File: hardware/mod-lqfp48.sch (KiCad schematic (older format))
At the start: 11 parts, among them J1 Target, U1 STM32F103C8Tx, Y1 8MHz

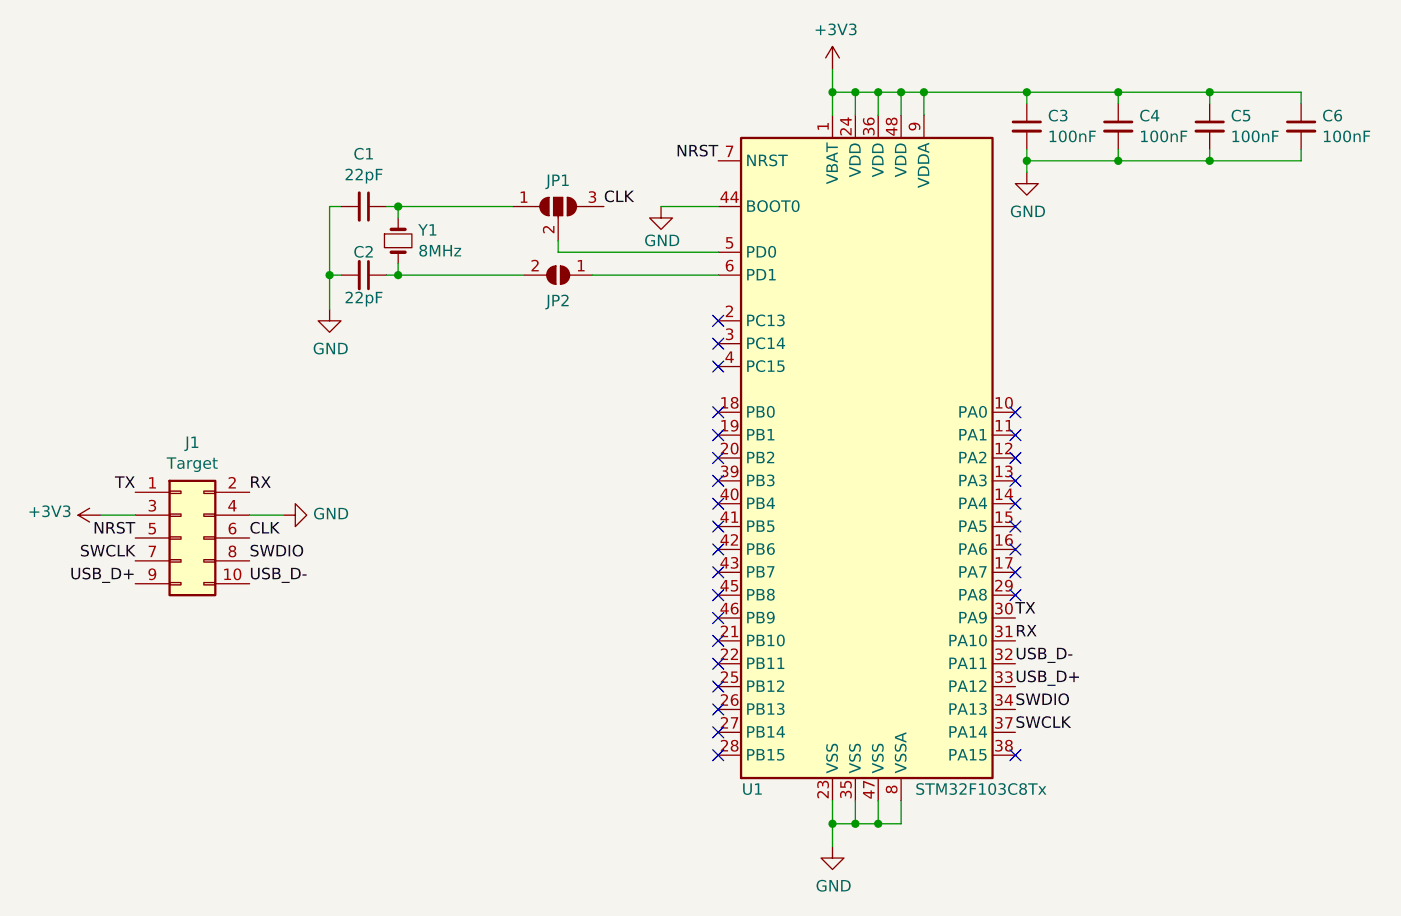
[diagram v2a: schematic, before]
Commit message: mod-lqfp48 is finally routed
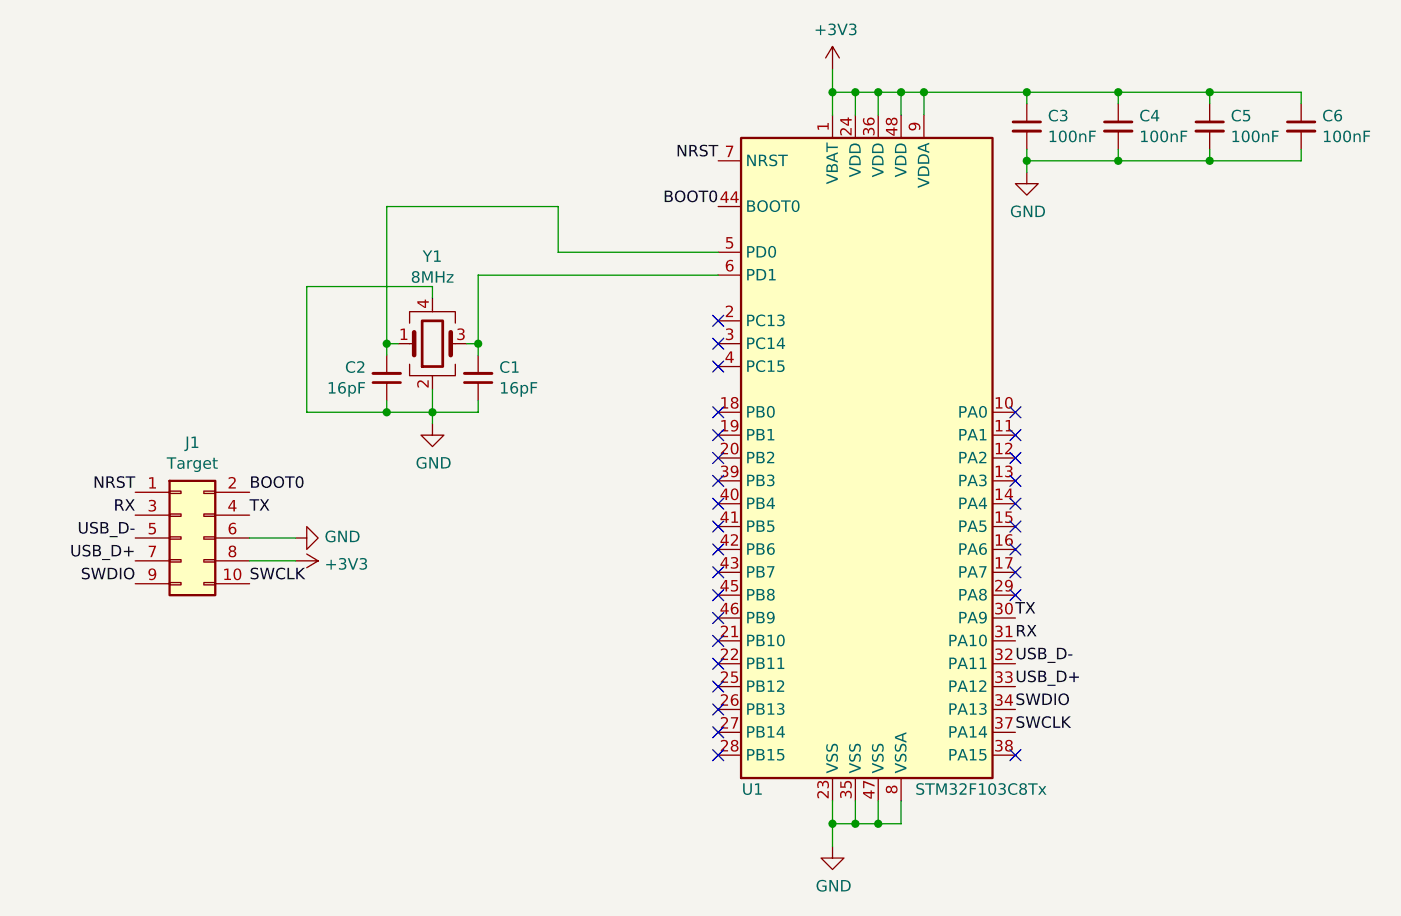
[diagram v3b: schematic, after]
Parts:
- removed JP1: SolderJumper_3_Open, Jumper:SolderJumper-3_P2.0mm_Open_TrianglePad1.0x1.5mm, symbol Jumper:SolderJumper_3_Open
- removed JP2: SolderJumper_2_Open, Jumper:SolderJumper-2_P1.3mm_Open_TrianglePad1.0x1.5mm, symbol Jumper:SolderJumper_2_Open
- removed Y1: 8MHz, Crystal:Crystal_HC18-U_Vertical, symbol Device:Crystal_Small
- added Y1: 8MHz, Crystal:Crystal_SMD_5032-4Pin_5.0x3.2mm, symbol Device:Crystal_GND24
- C1, C2: value 22pF -> 16pF
- J1: footprint Connector_PinHeader_2.54mm:PinHeader_2x05_P2.54mm_Horizontal -> unsorted:BH-10-Edge
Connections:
- net CLK is gone; now on net GND: J1.6 (Pin_6)
- net +3V3: now also J1.8 (Pin_8); no longer J1.3 (Pin_3)
- net GND: now also C1.1, C2.1, Y1.2, Y1.4; no longer C1.2, C2.2, J1.4 (Pin_4), U1.44 (BOOT0)
- net NRST: now also J1.1 (Pin_1); no longer J1.5 (Pin_5)
- net RX: now also J1.3 (Pin_3); no longer J1.2 (Pin_2)
- net SWCLK: now also J1.10 (Pin_10); no longer J1.7 (Pin_7)
- net SWDIO: now also J1.9 (Pin_9); no longer J1.8 (Pin_8)
- net TX: now also J1.4 (Pin_4); no longer J1.1 (Pin_1)
- net USB_D+: now also J1.7 (Pin_7); no longer J1.9 (Pin_9)
- net USB_D-: now also J1.5 (Pin_5); no longer J1.10 (Pin_10)
- net at U1.5 (PD0): now also C2.2, Y1.1
- net at U1.6 (PD1): now also C1.2, Y1.3
- new net BOOT0: J1.2 (Pin_2), U1.44 (BOOT0)
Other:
- moved on the sheet: C1, C2
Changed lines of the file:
@@
 F 0 "J1" H 1600 4167 50  0000 C CNN
 F 1 "Target" H 1600 4076 50  0000 C CNN
-F 2 "Connector_PinHeader_2.54mm:PinHeader_2x05_P2.54mm_Horizontal" H 1550 3750 50  0001 C CNN
+F 2 "unsorted:BH-10-Edge" H 1550 3750 50  0001 C CNN
 F 3 "~" H 1550 3750 50  0001 C CNN
 	1    1550 3750
 	1    0    0    -1
 $EndComp
-Text Label 1850 3950 0    50   ~ 0
+Text Label 1350 3750 2    50   ~ 0
 USB_D-
-Text Label 1350 3950 2    50   ~ 0
+Text Label 1350 3850 2    50   ~ 0
 USB_D+
-Text Label 1850 3750 0    50   ~ 0
-CLK
-Text Label 1350 3750 2    50   ~ 0
+Text Label 1350 3550 2    50   ~ 0
 NRST
-Text Label 1850 3850 0    50   ~ 0
-SWDIO
-Text Label 1350 3550 2    50   ~ 0
+Text Label 1850 3650 0    50   ~ 0
 TX
-Text Label 1850 3550 0    50   ~ 0
+Text Label 1350 3650 2    50   ~ 0
 RX
 $Comp
@@
 Text Label 3900 2100 2    50   ~ 0
 NRST
-Text Label 3400 2300 0    50   ~ 0
-CLK
-$Comp
-L power:GND #PWR0101
-U 1 1 5E4C8CEE
-P 3650 2300
-F 0 "#PWR0101" H 3650 2050 50  0001 C CNN
-F 1 "GND" H 3655 2150 50  0000 C CNN
-F 2 "" H 3650 2300 50  0001 C CNN
-F 3 "" H 3650 2300 50  0001 C CNN
-	1    3650 2300
-	1    0    0    -1
-$EndComp
-Wire Wire Line
-	3650 2300 3900 2300
 Wire Wire Line
 	4400 1900 4400 1800
@@
 RX
 $Comp
-L Device:Crystal_Small Y1
-U 1 1 5E4CB724
-P 2500 2450
-F 0 "Y1" V 2454 2538 50  0000 L CNN
-F 1 "8MHz" V 2545 2538 50  0000 L CNN
-F 2 "Crystal:Crystal_HC18-U_Vertical" H 2500 2450 50  0001 C CNN
-F 3 "~" H 2500 2450 50  0001 C CNN
-	1    2500 2450
-	0    1    1    0
-$EndComp
-$Comp
 L Device:C_Small C1
 U 1 1 5E4CCAC3
-P 2350 2300
-F 0 "C1" V 2121 2300 50  0000 C CNN
-F 1 "22pF" V 2212 2300 50  0000 C CNN
-F 2 "Capacitor_SMD:C_0805_2012Metric_Pad1.15x1.40mm_HandSolder" H 2350 2300 50  0001 C CNN
-F 3 "~" H 2350 2300 50  0001 C CNN
-	1    2350 2300
-	0    1    1    0
+P 2850 3050
+F 0 "C1" H 2758 3004 50  0000 R CNN
+F 1 "16pF" H 2758 3095 50  0000 R CNN
+F 2 "Capacitor_SMD:C_0805_2012Metric_Pad1.15x1.40mm_HandSolder" H 2850 3050 50  0001 C CNN
+F 3 "~" H 2850 3050 50  0001 C CNN
+	1    2850 3050
+	-1   0    0    1
 $EndComp
 $Comp
 L Device:C_Small C2
 U 1 1 5E4CCCD9
-P 2350 2600
-F 0 "C2" V 2250 2600 50  0000 C CNN
-F 1 "22pF" V 2450 2600 50  0000 C CNN
-F 2 "Capacitor_SMD:C_0805_2012Metric_Pad1.15x1.40mm_HandSolder" H 2350 2600 50  0001 C CNN
-F 3 "~" H 2350 2600 50  0001 C CNN
-	1    2350 2600
-	0    1    1    0
-$EndComp
-Wire Wire Line
-	2500 2350 2500 2300
-Wire Wire Line
-	2500 2300 2450 2300
-Wire Wire Line
-	2500 2550 2500 2600
-Wire Wire Line
-	2500 2600 2450 2600
+P 2450 3050
+F 0 "C2" H 2541 3004 50  0000 L CNN
+F 1 "16pF" H 2541 3095 50  0000 L CNN
+F 2 "Capacitor_SMD:C_0805_2012Metric_Pad1.15x1.40mm_HandSolder" H 2450 3050 50  0001 C CNN
+F 3 "~" H 2450 3050 50  0001 C CNN
+	1    2450 3050
+	-1   0    0    1
+$EndComp
 $Comp
 L power:GND #PWR03
 U 1 1 5E4CEED8
-P 2200 2750
-F 0 "#PWR03" H 2200 2500 50  0001 C CNN
-F 1 "GND" H 2205 2577 50  0000 C CNN
-F 2 "" H 2200 2750 50  0001 C CNN
-F 3 "" H 2200 2750 50  0001 C CNN
-	1    2200 2750
-	1    0    0    -1
-$EndComp
-Wire Wire Line
-	2200 2600 2200 2300
-Wire Wire Line
-	2200 2300 2250 2300
-Connection ~ 2200 2600
-Wire Wire Line
-	2200 2600 2250 2600
-$Comp
-L Jumper:SolderJumper_3_Open JP1
-U 1 1 5E4D2661
-P 3200 2300
-F 0 "JP1" H 3200 2413 50  0000 C CNN
-F 1 "SolderJumper_3_Open" V 3155 2367 50  0001 L CNN
-F 2 "Jumper:SolderJumper-3_P2.0mm_Open_TrianglePad1.0x1.5mm" H 3200 2300 50  0001 C CNN
-F 3 "~" H 3200 2300 50  0001 C CNN
-	1    3200 2300
-	1    0    0    -1
-$EndComp
-Connection ~ 2500 2300
-$Comp
-L Jumper:SolderJumper_2_Open JP2
-U 1 1 5E4D4ECF
-P 3200 2600
-F 0 "JP2" H 3200 2713 50  0000 C CNN
-F 1 "SolderJumper_2_Open" V 3245 2668 50  0001 L CNN
-F 2 "Jumper:SolderJumper-2_P1.3mm_Open_TrianglePad1.0x1.5mm" H 3200 2600 50  0001 C CNN
-F 3 "~" H 3200 2600 50  0001 C CNN
-	1    3200 2600
-	-1   0    0    1
-$EndComp
-Wire Wire Line
-	3000 2300 2500 2300
-Connection ~ 2500 2600
-Wire Wire Line
-	2200 2750 2200 2600
-Wire Wire Line
-	3350 2600 3900 2600
-Wire Wire Line
-	3200 2450 3200 2500
+P 2650 3250
+F 0 "#PWR03" H 2650 3000 50  0001 C CNN
+F 1 "GND" H 2655 3077 50  0000 C CNN
+F 2 "" H 2650 3250 50  0001 C CNN
+F 3 "" H 2650 3250 50  0001 C CNN
+	1    2650 3250
+	1    0    0    -1
+$EndComp
 Wire Wire Line
 	3200 2500 3900 2500
-Wire Wire Line
-	2500 2600 3050 2600
 $Comp
 L Device:C_Small C3
@@
 L power:+3V3 #PWR01
 U 1 1 5E4E8EE9
-P 1200 3650
-F 0 "#PWR01" H 1200 3500 50  0001 C CNN
-F 1 "+3V3" V 1215 3778 50  0000 L CNN
-F 2 "" H 1200 3650 50  0001 C CNN
-F 3 "" H 1200 3650 50  0001 C CNN
-	1    1200 3650
-	0    -1   -1   0
+P 2050 3850
+F 0 "#PWR01" H 2050 3700 50  0001 C CNN
+F 1 "+3V3" V 2065 3978 50  0000 L CNN
+F 2 "" H 2050 3850 50  0001 C CNN
+F 3 "" H 2050 3850 50  0001 C CNN
+	1    2050 3850
+	0    1    1    0
 $EndComp
 $Comp
 L power:GND #PWR02
 U 1 1 5E4E942F
-P 2000 3650
-F 0 "#PWR02" H 2000 3400 50  0001 C CNN
-F 1 "GND" V 2005 3522 50  0000 R CNN
-F 2 "" H 2000 3650 50  0001 C CNN
-F 3 "" H 2000 3650 50  0001 C CNN
-	1    2000 3650
+P 2050 3750
+F 0 "#PWR02" H 2050 3500 50  0001 C CNN
+F 1 "GND" V 2055 3622 50  0000 R CNN
+F 2 "" H 2050 3750 50  0001 C CNN
+F 3 "" H 2050 3750 50  0001 C CNN
+	1    2050 3750
 	0    -1   -1   0
 $EndComp
@@
 NoConn ~ 5200 4700
 Wire Wire Line
-	1200 3650 1350 3650
-Wire Wire Line
-	2000 3650 1850 3650
-Text Label 1350 3850 2    50   ~ 0
+	2050 3850 1850 3850
+Wire Wire Line
+	2050 3750 1850 3750
+Text Label 1850 3950 0    50   ~ 0
 SWCLK
+$Comp
+L Device:Crystal_GND24 Y1
+U 1 1 5E45E0AA
+P 2650 2900
+F 0 "Y1" H 2650 2519 50  0000 C CNN
+F 1 "8MHz" H 2650 2610 50  0000 C CNN
+F 2 "Crystal:Crystal_SMD_5032-4Pin_5.0x3.2mm" H 2650 2900 50  0001 C CNN
+F 3 "~" H 2650 2900 50  0001 C CNN
+	1    2650 2900
+	1    0    0    1
+$EndComp
+Wire Wire Line
+	2500 2900 2450 2900
+Wire Wire Line
+	2450 2900 2450 2950
+Wire Wire Line
+	2800 2900 2850 2900
+Wire Wire Line
+	2850 2900 2850 2950
+Wire Wire Line
+	2450 3150 2450 3200
+Wire Wire Line
+	2450 3200 2650 3200
+Wire Wire Line
+	2850 3200 2850 3150
+Wire Wire Line
+	2650 3100 2650 3200
+Connection ~ 2650 3200
+Wire Wire Line
+	2650 3200 2850 3200
+Wire Wire Line
+	2650 3250 2650 3200
+Wire Wire Line
+	2650 2700 2650 2650
+Wire Wire Line
+	2650 2650 2100 2650
+Wire Wire Line
+	2100 2650 2100 3200
+Wire Wire Line
+	2100 3200 2450 3200
+Connection ~ 2450 3200
+Wire Wire Line
+	2850 2900 2850 2600
+Connection ~ 2850 2900
+Wire Wire Line
+	2450 2900 2450 2300
+Connection ~ 2450 2900
+Text Label 1350 3950 2    50   ~ 0
+SWDIO
+Wire Wire Line
+	3200 2300 3200 2500
+Wire Wire Line
+	2450 2300 3200 2300
+Wire Wire Line
+	2850 2600 3900 2600
+Text Label 1850 3550 0    50   ~ 0
+BOOT0
+Text Label 3900 2300 2    50   ~ 0
+BOOT0
 $EndSCHEMATC
